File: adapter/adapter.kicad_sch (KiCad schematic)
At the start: 26 parts, among them J1 Serial, J2 Ribbon, J3 RGB, J4 Ribbon, J5 Battery charge, SW1 SW_SPST, SW3 SW_SPDT, U1 Dual MCU: RP2040 + nice!nano, U2 AP1603WG-7

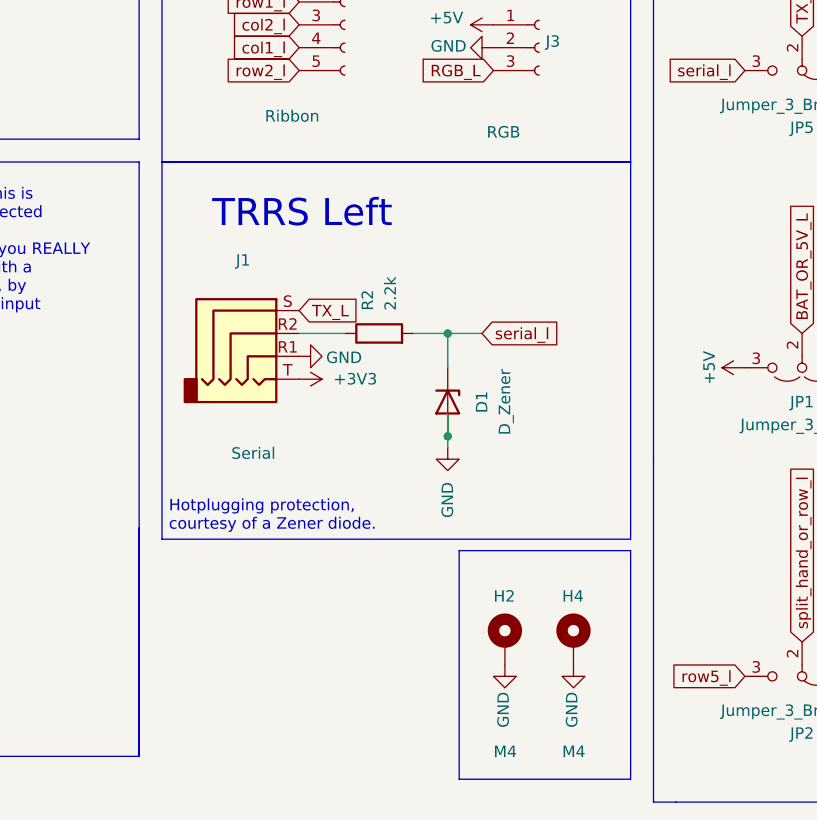
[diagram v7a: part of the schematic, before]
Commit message: sch: replace zener diode + resistor with TVS
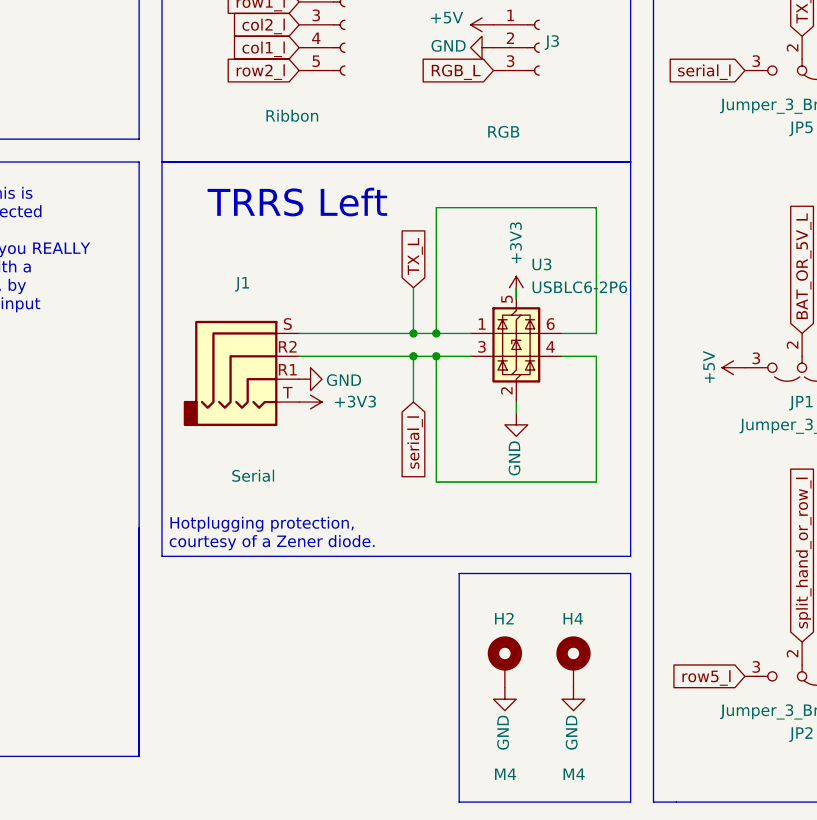
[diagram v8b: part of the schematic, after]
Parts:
- removed D1: D_Zener, symbol Device:D_Zener
- removed R2: 2.2k, library:R_1206_handsolder, symbol Device:R
- added U3: USBLC6-2P6, Package_TO_SOT_SMD:SOT-23-6, symbol Power_Protection:USBLC6-2SC6
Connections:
- net +3V3: now also U3.5 (VBUS)
- net GND: now also U3.2 (GND)
- net TX_L: now also U3.1 (I/O1), U3.6 (I/O1)
- net serial_l: now also J1.R2, U3.3 (I/O2), U3.4 (I/O2)
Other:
- moved on the sheet: H2, H4, J1
